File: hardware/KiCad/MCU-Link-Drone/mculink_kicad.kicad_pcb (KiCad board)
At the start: 2 copper layers, 50.1 x 43 mm, 107 parts, among them J1 USB_B_Micro, J2 Conn_02x03_Odd_Even, J3 Jumper_2_Open, J4 Jumper_2_Open, J5 Jumper_2_Open, J6 Conn_02x05_Odd_Even, J7 1x3pos, 100mil pitch, J8 Conn_01x04_Male, SW1 KMR221GLFS, U1 LPC55S69JBD64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

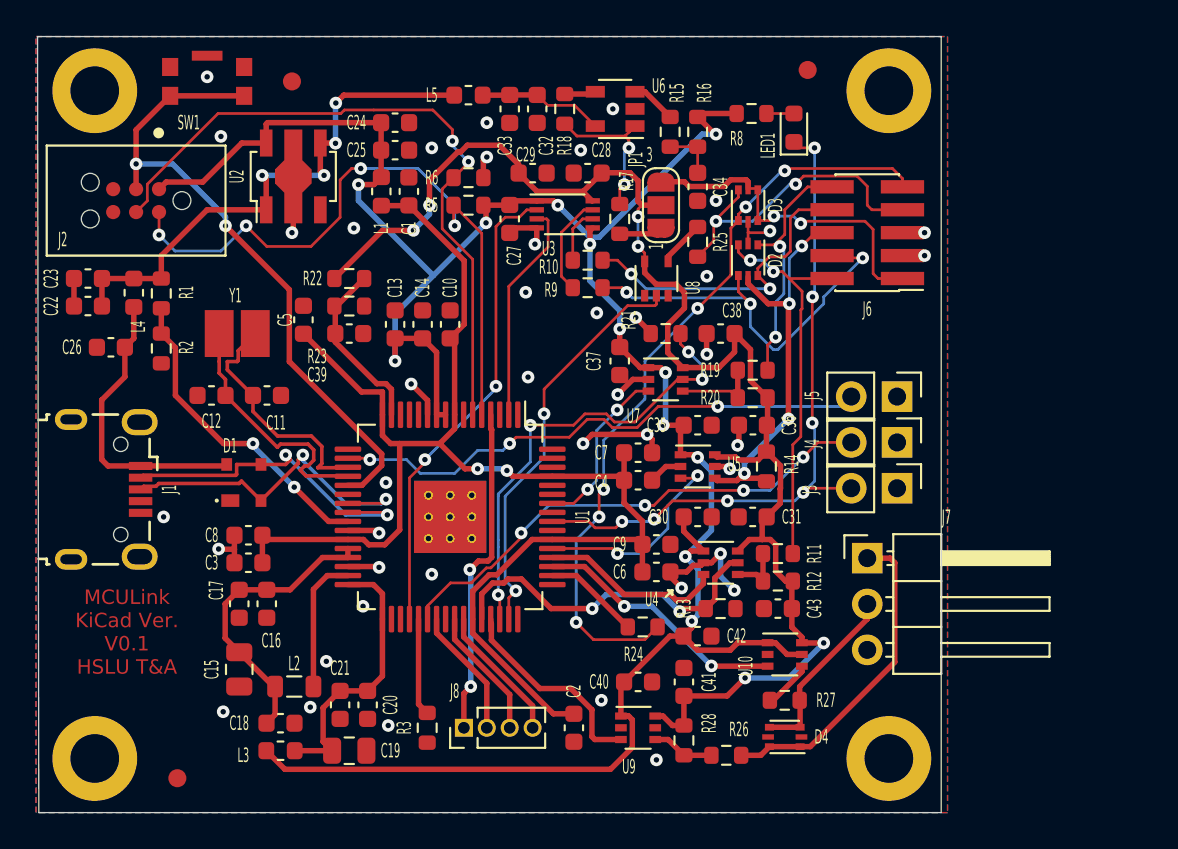
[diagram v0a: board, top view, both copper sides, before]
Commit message: updated with drone project files
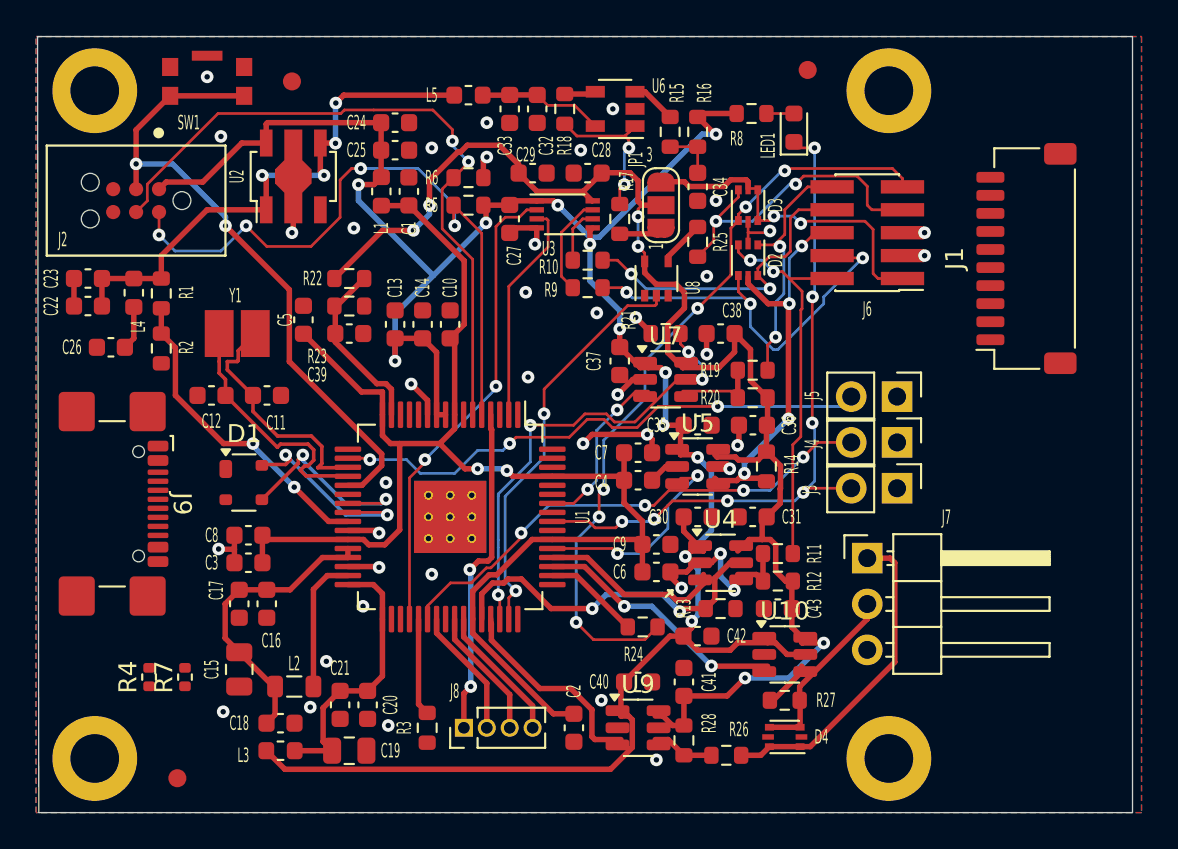
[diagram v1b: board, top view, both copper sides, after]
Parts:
- added J9: USB4110-GF-A_REVB, Connector_USB:USB_C_Receptacle_GCT_USB4110, F.Cu at (166.8, 101.9)
- added R4: 5k1, Resistor_SMD:R_0402_1005Metric, F.Cu at (170.0, 111.5)
- added R7: 5k1, Resistor_SMD:R_0402_1005Metric, F.Cu at (172.0, 111.5)
- D1: footprint mculink_kicad:SOT143B -> Package_TO_SOT_SMD:SOT-143
- J1: value USB_B_Micro -> Conn_01x10; footprint Connector_USB:USB_Micro-B_Wuerth_629105150521 -> Connector_JST:JST_SH_SM10B-SRSS-TB_1x10-1MP_P1.00mm_Horizontal
- U10, U4, U5, U7, U9: footprint Package_TO_SOT_SMD:SOT-363_SC-70-6 -> Package_TO_SOT_SMD:SOT-23-6
- moved J1 52.6 mm to (218.6, 88.3), turned to 90 degrees
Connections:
- net PIO0_11-SWDCLK renamed LPC_SWDCLK
- net PIO0_12-SWDIO renamed LPC_SWDIO
- D4 pad 5: Net-(D4-Pad5) -> unconnected-(D4D-K4-Pad5)
- J1 pad 1: /McuLink Power and USB/USB_VBUS -> /Debug interface/VTARGET
- J1 pad 2: /McuLink Power and USB/USB_D- -> FC0_TARGET_RXD
- J1 pad 3: /McuLink Power and USB/USB_D+ -> FCO_TARGET_TXD
- J1 pad 4: Net-(J1-Pad4) -> /Debug interface/IF_SWDIO
- J1 pad 5: GND -> /Debug interface/IF_SWCLK
- J1 pad 6: GND -> /Debug interface/IF_SWO
- J2 pad 6: Net-(J2-Pad6) -> unconnected-(J2-Pin_6-Pad6)
- U1 pad 1: Net-(U1-Pad1) -> unconnected-(U1C-PIO0_7-Pad1)
- U1 pad 12: Net-(U1-Pad12) -> unconnected-(U1C-PIO0_23-Pad12)
- U1 pad 13: PIO0_10-SWO -> unconnected-(U1C-PIO0_10-Pad13)
- U1 pad 14: Net-(U1-Pad14) -> unconnected-(U1C-PIO0_15-Pad14)
- U1 pad 17: Net-(U1-Pad17) -> unconnected-(U1C-PIO0_8-Pad17)
- U1 pad 3: Net-(U1-Pad3) -> unconnected-(U1C-PIO0_17-Pad3)
- U1 pad 34: Net-(U1-Pad34) -> unconnected-(U1A-XTAL32K_P-Pad34)
- U1 pad 35: Net-(U1-Pad35) -> unconnected-(U1A-XTAL32K_N-Pad35)
- U1 pad 40: Net-(U1-Pad40) -> unconnected-(U1C-PIO0_26-Pad40)
- U1 pad 48: Net-(U1-Pad48) -> unconnected-(U1C-PIO0_20-Pad48)
- U1 pad 49: Net-(U1-Pad49) -> unconnected-(U1C-PIO0_21-Pad49)
- U1 pad 55: Net-(U1-Pad55) -> unconnected-(U1C-PIO0_4-Pad55)
- U1 pad 57: Net-(U1-Pad57) -> unconnected-(U1C-PIO0_6-Pad57)
- U1 pad 59: Net-(U1-Pad59) -> unconnected-(U1C-PIO0_29-Pad59)
- U1 pad 60: Net-(U1-Pad60) -> unconnected-(U1C-PIO0_30-Pad60)
- U1 pad 62: Net-(U1-Pad62) -> unconnected-(U1B-USB0_DP-Pad62)
- U1 pad 63: Net-(U1-Pad63) -> unconnected-(U1B-USB0_DM-Pad63)
- U1 pad 7: Net-(U1-Pad7) -> unconnected-(U1C-PIO0_16-Pad7)
- U2 pad 3: Net-(U2-Pad3) -> unconnected-(U2-NC-Pad3)
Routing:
- net (no net): track 0.00 -> 16.0 mm
- net /McuLink Power and USB/USB_VBUS: track 16.3 -> 2.44 mm
- net Net-(D4B-K2): track 10.2 -> 0.00 mm
- net /McuLink Power and USB/USB_D+: track 19.0 -> 11.7 mm
- net /McuLink Power and USB/USB_D-: track 18.6 -> 11.3 mm
- net Net-(U4-B): track 3.08 -> 0.00 mm
- net Net-(U10-B): track 2.74 -> 0.00 mm
- net GND: track 41.3 -> 41.4 mm, vias 42 -> 41
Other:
- board size 50.1 x 43 mm -> 60.7 x 43 mm
- board text removed: "MCULink KiCad Ver. V0.1 HSLU T&A"

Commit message: worked on layout
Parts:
- removed J2: Conn_02x03_Odd_Even, mculink_kicad:TAG_TC2030-IDC-NL
- FID1, FID2, FID3: footprint mculink_kicad:Fiducial_1mm_Dia_2.54mm_Outer_CopperTop -> McuOnEclipse:Fiducial_1mm_Dia_2.54mm_Outer_CopperTop
- J4, J5: footprint Connector_PinHeader_2.54mm:PinHeader_1x02_P2.54mm_Vertical -> McuOnEclipse:SolderJumper-2_P1.3mm_Open_RoundedPad1.0x1.5mm
- J6: footprint mculink_kicad:SWD_Pin_Header_Straight_2x05_Pitch1.27mm_SMD -> McuOnEclipse:SWD_Pin_Header_Straight_2x05_Pitch1.27mm_SMD_Shrouded
- J7: footprint Connector_PinHeader_2.54mm:PinHeader_1x03_P2.54mm_Horizontal -> Connector_PinHeader_2.54mm:PinHeader_1x03_P2.54mm_Vertical
- J9: footprint Connector_USB:USB_C_Receptacle_GCT_USB4110 -> McuOnEclipse:USB_C_Receptacle_GCT_USB4110-GF-A
- U10, U4, U5, U7, U9: footprint Package_TO_SOT_SMD:SOT-23-6 -> Package_TO_SOT_SMD:SOT-363_SC-70-6
- moved H2 7.50 mm to (218.5, 79.0)
- moved H4 7.50 mm to (218.5, 116.0)
- moved FID1 4.50 mm to (211.0, 78.0)
- moved R7 4.00 mm to (168.0, 111.5)
- moved J9 2.26 mm to (167.9, 103.9)
- moved R4 1.01 mm to (169.0, 111.5)
- moved J1 0.71 mm to (218.5, 89.0)
- moved J6 0.66 mm to (210.5, 86.9), turned to 90 degrees
- moved J4 0.49 mm to (211.5, 98.0), turned to 180 degrees
- moved J5 0.45 mm to (211.5, 95.5), turned to 180 degrees
- moved J3 0.06 mm to (211.5, 101.1)
- turned D1 to 90 degrees
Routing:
- net FC0_TARGET_RXD: track 11.5 -> 55.2 mm, vias 0 -> 4
- net FCO_TARGET_TXD: track 14.2 -> 43.2 mm, vias 2 -> 4
- net (no net): track 16.0 -> 0.00 mm
- net /Debug interface/IF_SWO: track 22.5 -> 33.1 mm
- net Net-(J9-CC1): track 0.00 -> 10.2 mm
- net Net-(D4B-K2): track 0.00 -> 10.2 mm
- net /Debug interface/IF_RST: track 13.9 -> 23.0 mm
- net /Debug interface/IF_SWDIO: track 21.9 -> 30.8 mm, vias 2 -> 4
- net /McuLink Power and USB/USB_D-: track 11.3 -> 20.2 mm
- net /McuLink Power and USB/USB_D+: track 11.7 -> 19.5 mm
- net Net-(J9-CC2): track 0.00 -> 7.42 mm
- net LPC_SWDCLK: track 38.3 -> 44.9 mm, vias 2 -> 10
- net +3V3: track 133.8 -> 128.3 mm
- net /Debug interface/IF_SWCLK: track 22.5 -> 27.6 mm
- net Net-(D4A-K1): track 17.8 -> 22.1 mm
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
